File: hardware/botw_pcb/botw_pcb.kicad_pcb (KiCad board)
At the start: 2 copper layers, 65 x 36.3 mm, 71 parts, among them J1 Conn_02x03_Odd_Even, J2 Conn_01x03, M1 Motor_DC, M2 Motor_DC, M3 Motor_DC, M4 Motor_DC, M5 Motor_DC, M6 Motor_DC, M7 Motor_DC, M8 Motor_DC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

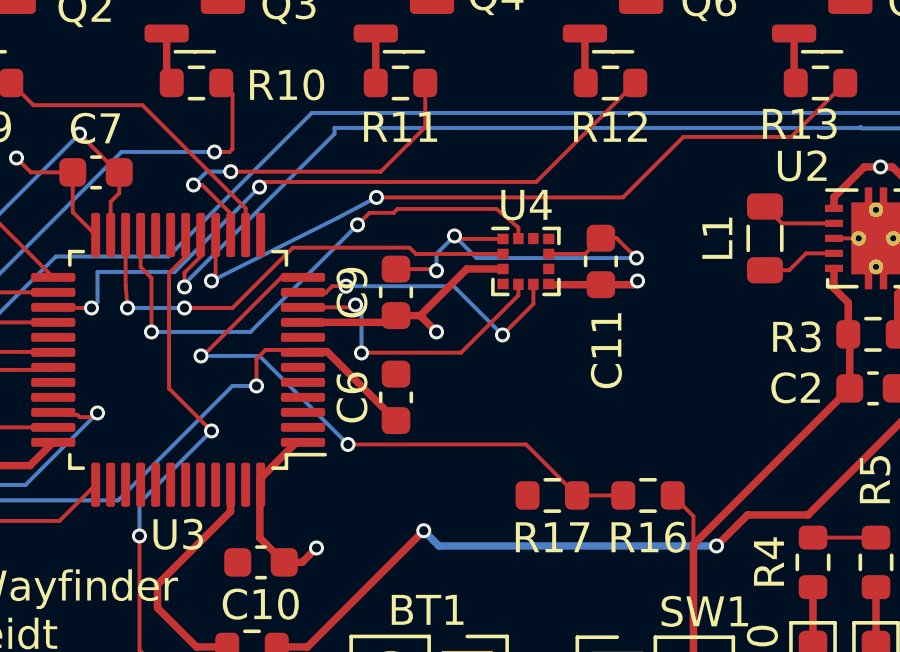
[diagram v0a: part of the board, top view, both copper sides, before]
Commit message: Added pullups to I2C'
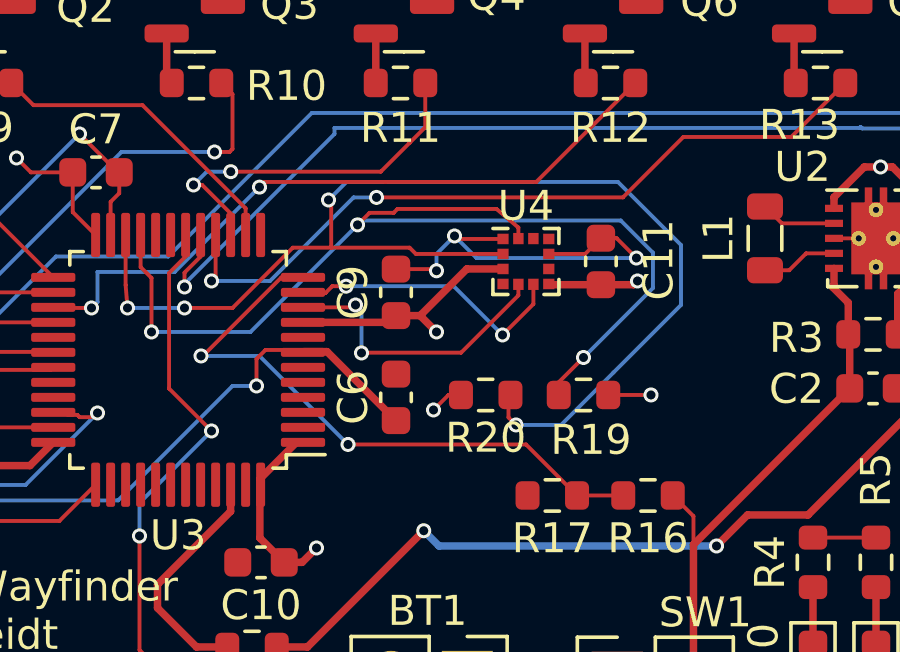
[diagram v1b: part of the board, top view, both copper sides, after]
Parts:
- added R19: 4k7, Resistor_SMD:R_0603_1608Metric, F.Cu at (86.5, 86.0)
- added R20: 4k7, Resistor_SMD:R_0603_1608Metric, F.Cu at (83.2, 86.0)
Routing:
- net SDA: track 15.9 -> 40.7 mm, vias 2 -> 4
- net SCL: track 17.9 -> 34.3 mm, vias 2 -> 3
- net +3.3V: track 86.5 -> 89.0 mm, vias 8 -> 10

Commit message: Changed to a new part for mag
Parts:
- removed REF** (x4): MountingHole_2.7mm_M2.5_DIN965, MountingHole:MountingHole_2.7mm_M2.5_DIN965
- added C12: 100n, Capacitor_SMD:C_0603_1608Metric, F.Cu at (90.7, 82.8)
- added C13: 100n, Capacitor_SMD:C_0603_1608Metric, F.Cu at (83.8, 80.3)
- added C14: 100n, Capacitor_SMD:C_0603_1608Metric, F.Cu at (86.5, 82.1)
- added C15: 100n, Capacitor_SMD:C_0603_1608Metric, F.Cu at (81.2, 81.5)
- added C16: 10u, Capacitor_SMD:C_0603_1608Metric, F.Cu at (88.8, 80.5)
- added H1: MountingHole, MountingHole:MountingHole_2.7mm_M2.5, F.Cu at (54.5, 65.0)
- added H2: MountingHole, MountingHole:MountingHole_2.7mm_M2.5, F.Cu at (54.5, 95.0)
- added H3: MountingHole, MountingHole:MountingHole_2.7mm_M2.5, F.Cu at (113.0, 81.0)
- added H4: MountingHole, MountingHole:MountingHole_2.7mm_M2.5, F.Cu at (113.0, 65.0)
- added TP1: TestPoint, TestPoint:TestPoint_Pad_D1.0mm, F.Cu at (60.0, 78.3)
- added TP2: TestPoint, TestPoint:TestPoint_Pad_D1.0mm, F.Cu at (57.6, 78.3)
- added U5: LSM6DS3, Package_LGA:LGA-14_3x2.5mm_P0.5mm_LayoutBorder3x4y, F.Cu at (83.8, 82.7)
- C1: value 1 uF -> 1u
- C10, C2, C6, C7, C8, C9: value 10 uF -> 10u
- C11: value 10 uF -> 220n
- C3: value 0.1 uF -> 0.1u
- C4, C5: value 10uF -> 10u
- L1: value 2.2uH -> 2.2u
- R10, R11, R12, R13, R14, R15, R18, R8, R9: value 2.2k -> 2k2
- U4: value MC6470 -> LIS2MDLTR
- moved U4 4.21 mm to (88.6, 82.8)
- moved R19 3.98 mm to (82.9, 87.7), turned to 90 degrees
- moved C11 3.94 mm to (88.8, 85.1), turned to 0 degrees
- moved R20 2.73 mm to (81.1, 87.7), turned to 90 degrees
- moved C6 1.07 mm to (79.2, 85.9)
- moved C9 1.07 mm to (79.2, 82.4)
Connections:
- net Net-(D11-Pad2) renamed /MCU/LED
- C11 pad 1: +3.3V -> Net-(C11-Pad1)
- R19 pad 1: SCL -> +3.3V
- R19 pad 2: +3.3V -> SDA
- R20 pad 1: SDA -> +3.3V
- R20 pad 2: +3.3V -> SCL
- U3 pad 10: INTA -> unconnected-(U3-Pad10)
- U3 pad 11: INTM -> unconnected-(U3-Pad11)
- U3 pad 42: unconnected-(U3-Pad42) -> DRDY
- U3 pad 43: unconnected-(U3-Pad43) -> INT2
- U3 pad 45: unconnected-(U3-Pad45) -> INT1
- U4 pad 1: GND -> SCL
- U4 pad 10: unconnected-(U4-Pad10) -> +3.3V
- U4 pad 12: SCL -> unconnected-(U4-Pad12)
- U4 pad 2: SDA -> unconnected-(U4-Pad2)
- U4 pad 4: unconnected-(U4-Pad4) -> SDA
- U4 pad 5: INTA -> Net-(C11-Pad1)
- U4 pad 6: INTM -> GND
- U4 pad 7: +3.3V -> DRDY
- U4 pad 8: unconnected-(U4-Pad8) -> GND
- U4 pad 9: GND -> +3.3V
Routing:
- net INT1: track 0.00 -> 29.4 mm, vias 0 -> 2
- net DRDY: track 0.00 -> 26.9 mm, vias 0 -> 2
- net INT2: track 0.00 -> 22.4 mm, vias 0 -> 2
- net +3.3V: track 89.0 -> 107.9 mm, vias 10 -> 12
- net SCL: track 34.3 -> 44.5 mm, vias 3 -> 5
- net INTA: track 9.86 -> 0.00 mm, vias 2 -> 0
- net INTM: track 9.54 -> 0.00 mm, vias 2 -> 0
- net Net-(C11-Pad1): track 0.00 -> 1.69 mm
- net GND: track 65.1 -> 63.6 mm, vias 5 -> 2
- net /MCU/LED: track 41.8 -> 43.3 mm
- net Net-(Q5-Pad2): track 28.8 -> 29.8 mm
- net SDA: track 40.7 -> 41.5 mm, vias 4 -> 3
- net NRST: track 31.9 -> 31.3 mm
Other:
- board text added: "- +"

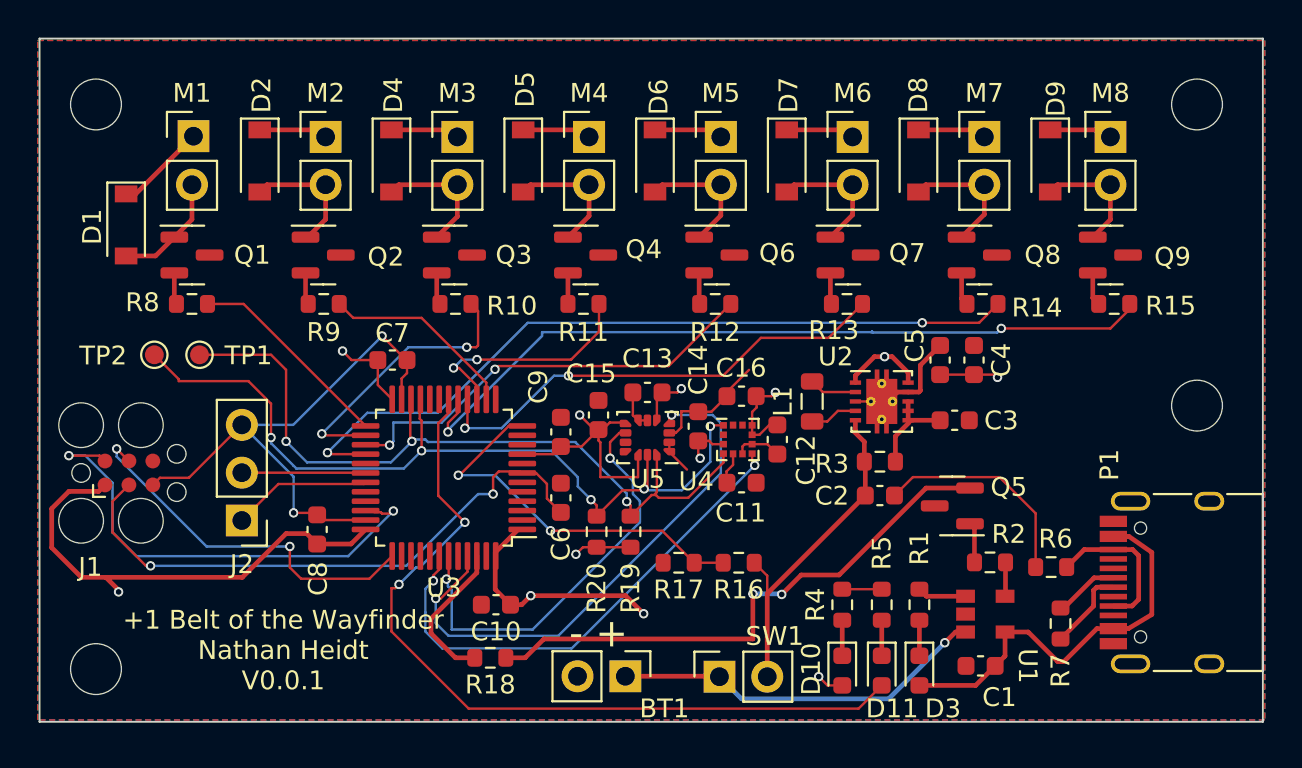
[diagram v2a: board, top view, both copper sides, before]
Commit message: Transistor footprint was wrong, whoops! Also added in hard iron correction
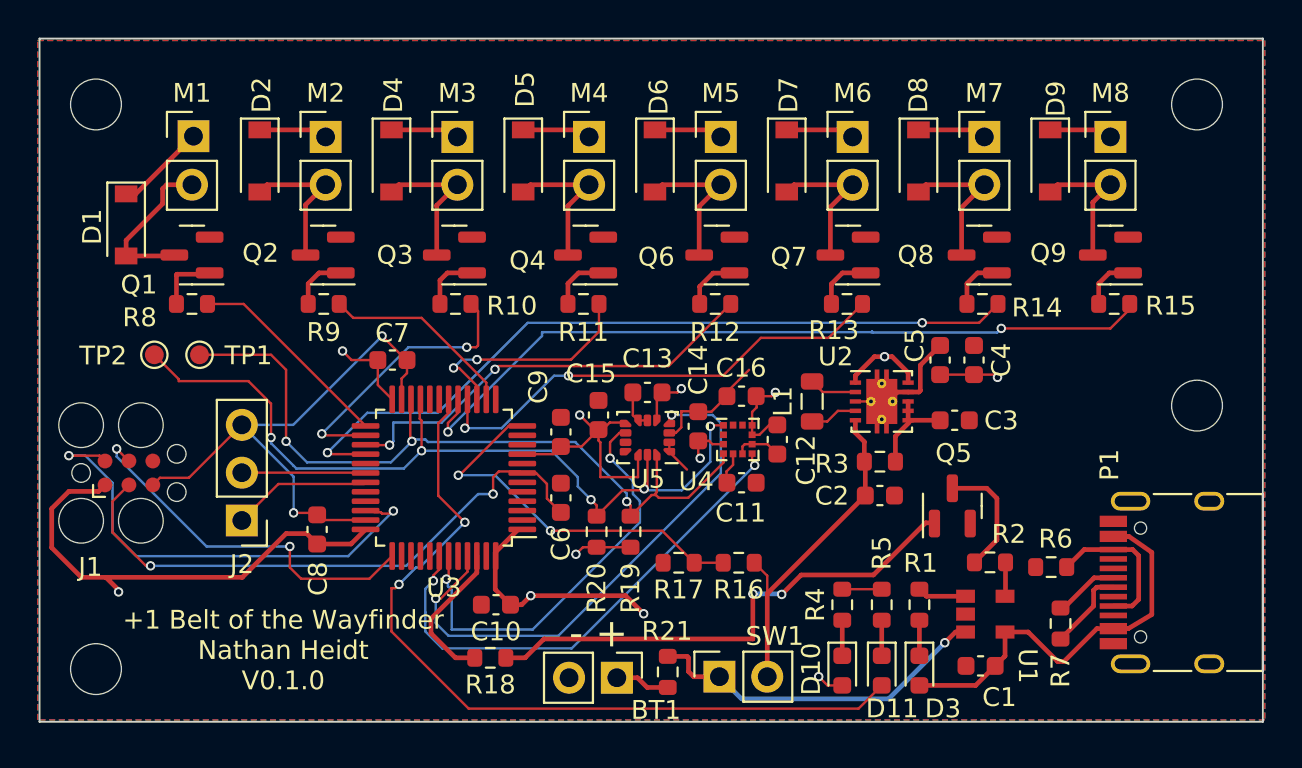
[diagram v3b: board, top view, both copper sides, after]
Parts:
- added G***: LOGO, LOGO, B.Cu at (98.1, 80.7)
- added R21: 0, Resistor_SMD:R_0603_1608Metric, F.Cu at (84.9, 95.2)
- moved BT1 0.46 mm to (82.2, 95.5)
- turned Q1 to 180 degrees
- turned Q2 to 180 degrees
- turned Q3 to 180 degrees
- turned Q4 to 180 degrees
- turned Q5 to 90 degrees
- turned Q6 to 180 degrees
- turned Q7 to 180 degrees
- turned Q8 to 180 degrees
- turned Q9 to 180 degrees
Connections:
- BT1 pad 1: +BATT -> Net-(BT1-Pad1)
- Q1 pad 1: Net-(D1-Pad2) -> Net-(R8-Pad1)
- Q1 pad 2: Net-(Q1-Pad2) -> GND
- Q1 pad 3: GND -> Net-(D1-Pad2)
- Q2 pad 1: Net-(D2-Pad2) -> Net-(R9-Pad1)
- Q2 pad 2: Net-(Q2-Pad2) -> GND
- Q2 pad 3: GND -> Net-(D2-Pad2)
- Q3 pad 1: Net-(D4-Pad2) -> Net-(R10-Pad1)
- Q3 pad 2: Net-(Q3-Pad2) -> GND
- Q3 pad 3: GND -> Net-(D4-Pad2)
- Q4 pad 1: Net-(D5-Pad2) -> Net-(R11-Pad1)
- Q4 pad 2: Net-(Q4-Pad2) -> GND
- Q4 pad 3: GND -> Net-(D5-Pad2)
- Q5 pad 1: Net-(Q5-Pad1) -> Net-(R18-Pad1)
- Q5 pad 2: Net-(Q5-Pad2) -> GND
- Q5 pad 3: GND -> Net-(R2-Pad2)
- Q6 pad 1: Net-(D6-Pad2) -> Net-(R12-Pad1)
- Q6 pad 2: Net-(Q6-Pad2) -> GND
- Q6 pad 3: GND -> Net-(D6-Pad2)
- Q7 pad 1: Net-(D7-Pad2) -> Net-(R13-Pad1)
- Q7 pad 2: Net-(Q7-Pad2) -> GND
- Q7 pad 3: GND -> Net-(D7-Pad2)
- Q8 pad 1: Net-(D8-Pad2) -> Net-(R14-Pad1)
- Q8 pad 2: Net-(Q8-Pad2) -> GND
- Q8 pad 3: GND -> Net-(D8-Pad2)
- Q9 pad 1: Net-(D9-Pad2) -> Net-(R15-Pad1)
- Q9 pad 2: Net-(Q9-Pad2) -> GND
- Q9 pad 3: GND -> Net-(D9-Pad2)
- R10 pad 1: Net-(Q3-Pad2) -> Net-(R10-Pad1)
- R11 pad 1: Net-(Q4-Pad2) -> Net-(R11-Pad1)
- R12 pad 1: Net-(Q6-Pad2) -> Net-(R12-Pad1)
- R13 pad 1: Net-(Q7-Pad2) -> Net-(R13-Pad1)
- R14 pad 1: Net-(Q8-Pad2) -> Net-(R14-Pad1)
- R15 pad 1: Net-(Q9-Pad2) -> Net-(R15-Pad1)
- R18 pad 1: Net-(Q5-Pad2) -> Net-(R18-Pad1)
- R2 pad 2: Net-(Q5-Pad1) -> Net-(R2-Pad2)
- R8 pad 1: Net-(Q1-Pad2) -> Net-(R8-Pad1)
- R9 pad 1: Net-(Q2-Pad2) -> Net-(R9-Pad1)
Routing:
- net Net-(Q5-Pad2): track 29.8 -> 0.00 mm, vias 2 -> 0
- net Net-(R18-Pad1): track 0.00 -> 27.2 mm, vias 0 -> 2
- net GND: track 63.6 -> 52.0 mm
- net Net-(R2-Pad2): track 0.00 -> 6.49 mm
- net Net-(R8-Pad1): track 0.00 -> 3.35 mm
- net Net-(R11-Pad1): track 0.00 -> 3.20 mm
- net Net-(R13-Pad1): track 0.00 -> 3.13 mm
- net Net-(R10-Pad1): track 0.00 -> 3.12 mm
- net Net-(R12-Pad1): track 0.00 -> 3.07 mm
- net Net-(R9-Pad1): track 0.00 -> 3.05 mm
- net Net-(BT1-Pad1): track 0.00 -> 2.92 mm
- net Net-(R14-Pad1): track 0.00 -> 2.91 mm
- net Net-(R15-Pad1): track 0.00 -> 2.88 mm
- net Net-(D1-Pad2): track 6.15 -> 8.61 mm
- net Net-(Q5-Pad1): track 2.15 -> 0.00 mm
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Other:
- board text added: "+1 Belt of the Wayfinder Nathan Heidt V0.1.0"
- board text removed: "+1 Belt of the Wayfinder Nathan Heidt V0.0.1"
